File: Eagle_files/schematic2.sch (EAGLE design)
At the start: 76 parts, among them IC6 DS3231/SO

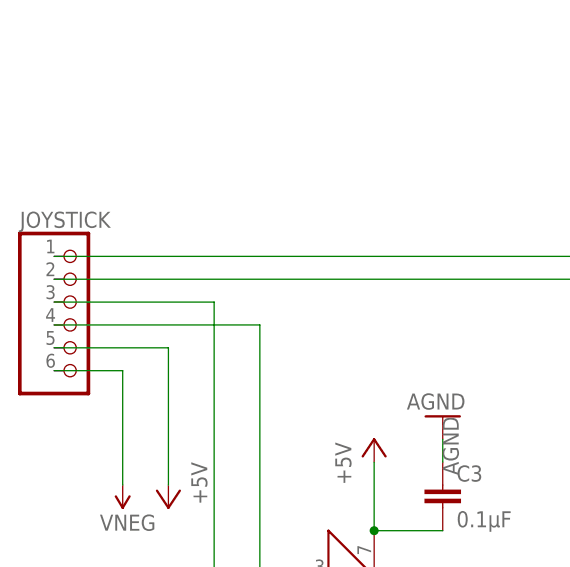
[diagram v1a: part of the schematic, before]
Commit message: I don't think I fixed much on this version, move to RevB for actual fixes.
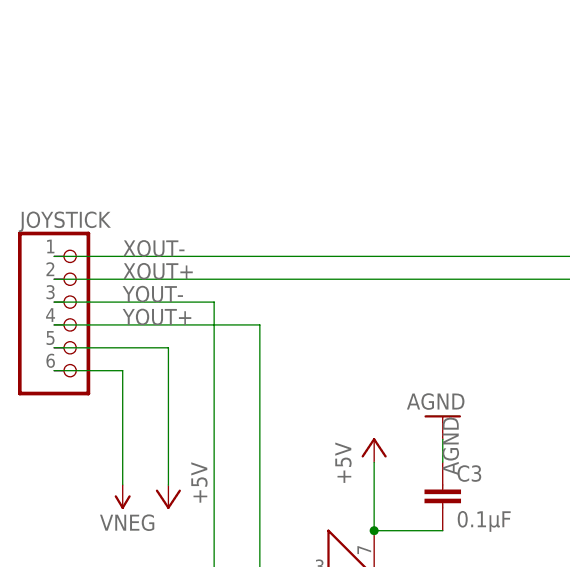
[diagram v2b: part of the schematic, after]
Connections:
- net N$1 renamed XOUT+
- net N$19 renamed XOUT-
- net N$23 renamed YOUT-
- net N$24 renamed YOUT+
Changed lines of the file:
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@@
 <grid distance="0.1" unitdist="inch" unit="inch" style="lines" multiple="1" display="no" altdistance="0.01" altunitdist="inch" altunit="inch"/>
 <layers>
-<layer number="1" name="Top" color="4" fill="1" visible="yes" active="no"/>
-<layer number="16" name="Bottom" color="1" fill="1" visible="yes" active="no"/>
-<layer number="17" name="Pads" color="2" fill="1" visible="yes" active="no"/>
-<layer number="18" name="Vias" color="2" fill="1" visible="yes" active="no"/>
-<layer number="19" name="Unrouted" color="6" fill="1" visible="yes" active="no"/>
-<layer number="20" name="Dimension" color="15" fill="1" visible="yes" active="no"/>
-<layer number="21" name="tPlace" color="16" fill="1" visible="yes" active="no"/>
-<layer number="22" name="bPlace" color="14" fill="1" visible="yes" active="no"/>
-<layer number="23" name="tOrigins" color="15" fill="1" visible="yes" active="no"/>
-<layer number="24" name="bOrigins" color="15" fill="1" visible="yes" active="no"/>
-<layer number="25" name="tNames" color="7" fill="1" visible="yes" active="no"/>
-<layer number="26" name="bNames" color="7" fill="1" visible="yes" active="no"/>
-<layer number="27" name="tValues" color="7" fill="1" visible="yes" active="no"/>
-<layer number="28" name="bValues" color="7" fill="1" visible="yes" active="no"/>
+<layer number="1" name="Top" color="4" fill="1" visible="no" active="no"/>
+<layer number="16" name="Bottom" color="1" fill="1" visible="no" active="no"/>
+<layer number="17" name="Pads" color="2" fill="1" visible="no" active="no"/>
+<layer number="18" name="Vias" color="2" fill="1" visible="no" active="no"/>
+<layer number="19" name="Unrouted" color="6" fill="1" visible="no" active="no"/>
+<layer number="20" name="Dimension" color="15" fill="1" visible="no" active="no"/>
+<layer number="21" name="tPlace" color="16" fill="1" visible="no" active="no"/>
+<layer number="22" name="bPlace" color="14" fill="1" visible="no" active="no"/>
+<layer number="23" name="tOrigins" color="15" fill="1" visible="no" active="no"/>
+<layer number="24" name="bOrigins" color="15" fill="1" visible="no" active="no"/>
+<layer number="25" name="tNames" color="7" fill="1" visible="no" active="no"/>
+<layer number="26" name="bNames" color="7" fill="1" visible="no" active="no"/>
+<layer number="27" name="tValues" color="7" fill="1" visible="no" active="no"/>
+<layer number="28" name="bValues" color="7" fill="1" visible="no" active="no"/>
 <layer number="29" name="tStop" color="7" fill="3" visible="no" active="no"/>
 <layer number="30" name="bStop" color="7" fill="6" visible="no" active="no"/>
@@
 <layer number="35" name="tGlue" color="7" fill="4" visible="no" active="no"/>
 <layer number="36" name="bGlue" color="7" fill="5" visible="no" active="no"/>
-<layer number="37" name="tTest" color="7" fill="1" visible="yes" active="no"/>
-<layer number="38" name="bTest" color="7" fill="1" visible="yes" active="no"/>
+<layer number="37" name="tTest" color="7" fill="1" visible="no" active="no"/>
+<layer number="38" name="bTest" color="7" fill="1" visible="no" active="no"/>
 <layer number="39" name="tKeepout" color="4" fill="11" visible="no" active="no"/>
 <layer number="40" name="bKeepout" color="1" fill="11" visible="no" active="no"/>
@@
 <layer number="44" name="Drills" color="7" fill="1" visible="no" active="no"/>
 <layer number="45" name="Holes" color="7" fill="1" visible="no" active="no"/>
-<layer number="46" name="Milling" color="3" fill="1" visible="yes" active="no"/>
-<layer number="47" name="Measures" color="7" fill="1" visible="yes" active="no"/>
-<layer number="48" name="Document" color="7" fill="1" visible="yes" active="no"/>
-<layer number="49" name="Reference" color="7" fill="1" visible="yes" active="no"/>
-<layer number="50" name="dxf" color="7" fill="1" visible="yes" active="no"/>
-<layer number="51" name="tDocu" color="6" fill="1" visible="yes" active="no"/>
-<layer number="52" name="bDocu" color="7" fill="1" visible="yes" active="no"/>
-<layer number="53" name="tGND_GNDA" color="7" fill="9" visible="yes" active="no"/>
-<layer number="54" name="bGND_GNDA" color="1" fill="9" visible="yes" active="no"/>
-<layer number="56" name="wert" color="7" fill="1" visible="yes" active="no"/>
-<layer number="57" name="tCAD" color="7" fill="1" visible="yes" active="no"/>
+<layer number="46" name="Milling" color="3" fill="1" visible="no" active="no"/>
+<layer number="47" name="Measures" color="7" fill="1" visible="no" active="no"/>
+<layer number="48" name="Document" color="7" fill="1" visible="no" active="no"/>
+<layer number="49" name="Reference" color="7" fill="1" visible="no" active="no"/>
+<layer number="50" name="dxf" color="7" fill="1" visible="no" active="no"/>
+<layer number="51" name="tDocu" color="6" fill="1" visible="no" active="no"/>
+<layer number="52" name="bDocu" color="7" fill="1" visible="no" active="no"/>
+<layer number="53" name="tGND_GNDA" color="7" fill="9" visible="no" active="no"/>
+<layer number="54" name="bGND_GNDA" color="1" fill="9" visible="no" active="no"/>
+<layer number="56" name="wert" color="7" fill="1" visible="no" active="no"/>
+<layer number="57" name="tCAD" color="7" fill="1" visible="no" active="no"/>
 <layer number="90" name="Modules" color="5" fill="1" visible="yes" active="yes"/>
 <layer number="91" name="Nets" color="2" fill="1" visible="yes" active="yes"/>
@@
 </segment>
 </net>
-<net name="N$19" class="0">
+<net name="XOUT-" class="0">
 <segment>
 <wire x1="96.52" y1="200.66" x2="96.52" y2="172.72" width="0.1524" layer="91"/>
@@
 <pinref part="JOYSTICK" gate="A" pin="1"/>
 <wire x1="-2.54" y1="200.66" x2="96.52" y2="200.66" width="0.1524" layer="91"/>
+<label x="5.08" y="200.66" size="1.778" layer="95"/>
 </segment>
 </net>
@@
 </segment>
 </net>
-<net name="N$23" class="0">
+<net name="YOUT-" class="0">
 <segment>
 <wire x1="-2.54" y1="195.58" x2="15.24" y2="195.58" width="0.1524" layer="91"/>
@@
 <pinref part="JOY_Y" gate="G$1" pin="-"/>
 <wire x1="15.24" y1="144.78" x2="25.4" y2="144.78" width="0.1524" layer="91"/>
-</segment>
-</net>
-<net name="N$24" class="0">
+<label x="5.08" y="195.58" size="1.778" layer="95"/>
+</segment>
+</net>
+<net name="YOUT+" class="0">
 <segment>
 <wire x1="-2.54" y1="193.04" x2="20.32" y2="193.04" width="0.1524" layer="91"/>
@@
 <pinref part="JOY_Y" gate="G$1" pin="+"/>
 <wire x1="20.32" y1="165.1" x2="25.4" y2="165.1" width="0.1524" layer="91"/>
+<label x="5.08" y="193.04" size="1.778" layer="95"/>
 </segment>
 </net>
@@
 </segment>
 </net>
-<net name="N$1" class="0">
+<net name="XOUT+" class="0">
 <segment>
 <pinref part="JOYSTICK" gate="A" pin="2"/>
@@
 <wire x1="-2.54" y1="198.12" x2="109.22" y2="198.12" width="0.1524" layer="91"/>
 <wire x1="109.22" y1="198.12" x2="109.22" y2="193.04" width="0.1524" layer="91"/>
-</segment>
-</net>
+<label x="5.08" y="198.12" size="1.778" layer="95"/>
+</segment>
+</net>
